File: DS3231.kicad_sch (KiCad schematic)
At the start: 8 parts, among them IC1 DS3231, J1 Conn_01x08_Pin

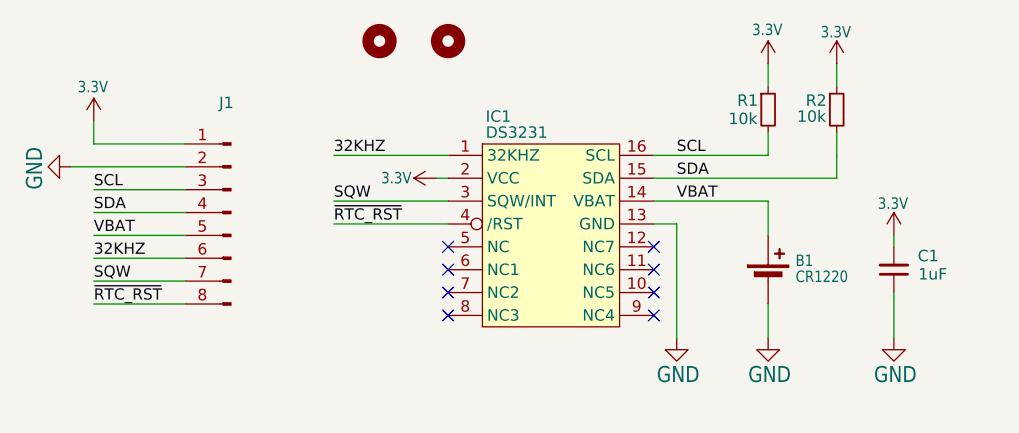
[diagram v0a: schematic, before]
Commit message: fix(sch): add PWR_FLAG on 3.3V and GND
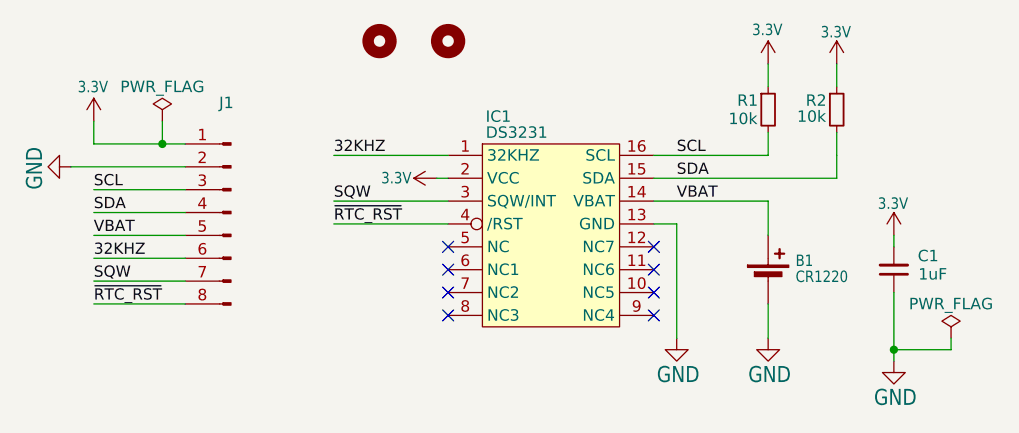
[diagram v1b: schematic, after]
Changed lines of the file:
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@@
 		(date "2024-03-06")
+	)
+	(junction
+		(at 116.84 91.44)
+		(diameter 0)
+		(color 0 0 0 0)
+	)
+	(junction
+		(at 198.12 114.3)
+		(diameter 0)
+		(color 0 0 0 0)
 	)
 	(no_connect
@@
 	(wire
 		(pts
+			(xy 204.47 114.3) (xy 198.12 114.3)
+		)
+		(stroke
+			(width 0)
+			(type default)
+		)
+	)
+	(wire
+		(pts
+			(xy 204.47 113.03) (xy 204.47 114.3)
+		)
+		(stroke
+			(width 0)
+			(type default)
+		)
+	)
+	(wire
+		(pts
 			(xy 109.22 104.14) (xy 119.38 104.14)
 		)
@@
 	(wire
 		(pts
-			(xy 184.15 109.22) (xy 184.15 113.03)
+			(xy 116.84 88.9) (xy 116.84 91.44)
 		)
 		(stroke
@@
 	(wire
 		(pts
-			(xy 119.38 101.6) (xy 109.22 101.6)
+			(xy 184.15 109.22) (xy 184.15 113.03)
+		)
+		(stroke
+			(width 0)
+			(type default)
+		)
+	)
+	(wire
+		(pts
+			(xy 116.84 91.44) (xy 119.38 91.44)
 		)
 		(stroke
@@
 	(wire
 		(pts
-			(xy 135.89 92.71) (xy 148.59 92.71)
+			(xy 119.38 101.6) (xy 109.22 101.6)
 		)
 		(stroke
@@
 	(wire
 		(pts
-			(xy 191.77 95.25) (xy 191.77 92.71)
+			(xy 135.89 92.71) (xy 148.59 92.71)
 		)
 		(stroke
@@
 	(wire
 		(pts
+			(xy 191.77 95.25) (xy 191.77 92.71)
+		)
+		(stroke
+			(width 0.1524)
+			(type solid)
+		)
+	)
+	(wire
+		(pts
 			(xy 184.15 90.17) (xy 184.15 92.71)
 		)
@@
 	(wire
 		(pts
-			(xy 147.32 95.25) (xy 148.59 95.25)
+			(xy 198.12 114.3) (xy 198.12 115.57)
 		)
 		(stroke
@@
 	(wire
 		(pts
-			(xy 198.12 107.95) (xy 198.12 113.03)
+			(xy 147.32 95.25) (xy 148.59 95.25)
 		)
 		(stroke
@@
 	(wire
 		(pts
+			(xy 198.12 107.95) (xy 198.12 114.3)
+		)
+		(stroke
+			(width 0)
+			(type default)
+		)
+	)
+	(wire
+		(pts
 			(xy 135.89 97.79) (xy 148.59 97.79)
 		)
@@
 	(wire
 		(pts
-			(xy 109.22 91.44) (xy 119.38 91.44)
+			(xy 109.22 91.44) (xy 116.84 91.44)
 		)
 		(stroke
@@
 				(path "/3054a26c-491b-4a2c-bd9e-2e89ff40ccf1"
 					(reference "#U$02")
+					(unit 1)
+				)
+			)
+		)
+	)
+	(symbol
+		(lib_id "power:PWR_FLAG")
+		(at 204.47 113.03 0)
+		(unit 1)
+		(body_style 1)
+		(exclude_from_sim no)
+		(in_bom yes)
+		(on_board yes)
+		(in_pos_files yes)
+		(dnp no)
+		(property "Reference" "#FLG02"
+			(at 204.47 111.125 0)
+			(hide yes)
+			(show_name no)
+			(do_not_autoplace no)
+			(effects
+				(font
+					(size 1.27 1.27)
+				)
+			)
+		)
+		(property "Value" "PWR_FLAG"
+			(at 204.47 109.22 0)
+			(show_name no)
+			(do_not_autoplace no)
+			(effects
+				(font
+					(size 1.27 1.27)
+				)
+			)
+		)
+		(property "Footprint" ""
+			(at 204.47 113.03 0)
+			(hide yes)
+			(show_name no)
+			(do_not_autoplace no)
+			(effects
+				(font
+					(size 1.27 1.27)
+				)
+			)
+		)
+		(property "Datasheet" ""
+			(at 204.47 113.03 0)
+			(hide yes)
+			(show_name no)
+			(do_not_autoplace no)
+			(effects
+				(font
+					(size 1.27 1.27)
+				)
+			)
+		)
+		(property "Description" "Special symbol for telling ERC where power comes from"
+			(at 204.47 113.03 0)
+			(hide yes)
+			(show_name no)
+			(do_not_autoplace no)
+			(effects
+				(font
+					(size 1.27 1.27)
+				)
+			)
+		)
+		(pin "1"
+		)
+		(instances
+			(project "DS3231"
+				(path "/3054a26c-491b-4a2c-bd9e-2e89ff40ccf1"
+					(reference "#FLG02")
 					(unit 1)
 				)
@@
 	(symbol
 		(lib_id "power:GND")
-		(at 198.12 113.03 0)
+		(at 198.12 115.57 0)
 		(mirror y)
 		(unit 1)
@@
 		(dnp no)
 		(property "Reference" "#GND04"
-			(at 198.12 113.03 0)
+			(at 198.12 115.57 0)
 			(hide yes)
 			(show_name no)
@@
 		)
 		(property "Value" "GND"
-			(at 200.66 118.11 0)
+			(at 200.66 120.65 0)
 			(show_name no)
 			(do_not_autoplace no)
@@
 		)
 		(property "Footprint" ""
-			(at 198.12 113.03 0)
+			(at 198.12 115.57 0)
 			(hide yes)
 			(show_name no)
@@
 		)
 		(property "Datasheet" ""
-			(at 198.12 113.03 0)
+			(at 198.12 115.57 0)
 			(hide yes)
 			(show_name no)
@@
 		)
 		(property "Description" "Power symbol creates a global label with name \"GND\" , ground"
-			(at 198.12 113.03 0)
+			(at 198.12 115.57 0)
 			(hide yes)
 			(show_name no)
@@
 					(unit 1)
 				)
+			)
+		)
+	)
+	(symbol
+		(lib_id "power:PWR_FLAG")
+		(at 116.84 88.9 0)
+		(unit 1)
+		(body_style 1)
+		(exclude_from_sim no)
+		(in_bom yes)
+		(on_board yes)
+		(in_pos_files yes)
+		(dnp no)
+		(property "Reference" "#FLG01"
+			(at 116.84 86.995 0)
+			(hide yes)
+			(show_name no)
+			(do_not_autoplace no)
+			(effects
+				(font
+					(size 1.27 1.27)
+				)
+			)
+		)
+		(property "Value" "PWR_FLAG"
+			(at 116.84 85.09 0)
+			(show_name no)
+			(do_not_autoplace no)
+			(effects
+				(font
+					(size 1.27 1.27)
+				)
+			)
+		)
+		(property "Footprint" ""
+			(at 116.84 88.9 0)
+			(hide yes)
+			(show_name no)
+			(do_not_autoplace no)
+			(effects
+				(font
+					(size 1.27 1.27)
+				)
+			)
+		)
+		(property "Datasheet" ""
+			(at 116.84 88.9 0)
+			(hide yes)
+			(show_name no)
+			(do_not_autoplace no)
+			(effects
+				(font
+					(size 1.27 1.27)
+				)
+			)
+		)
+		(property "Description" "Special symbol for telling ERC where power comes from"
+			(at 116.84 88.9 0)
+			(hide yes)
+			(show_name no)
+			(do_not_autoplace no)
+			(effects
+				(font
+					(size 1.27 1.27)
+				)
+			)
+		)
+		(pin "1"
+		)
+		(instances
+			(project "DS3231"
+				(path "/3054a26c-491b-4a2c-bd9e-2e89ff40ccf1"
+					(reference "#FLG01")
+					(unit 1)
+				)
